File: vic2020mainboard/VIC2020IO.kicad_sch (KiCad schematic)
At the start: 45 parts, among them J10 5v Regulated, J11 Conn_02x08_Odd_Even, J12 Conn_02x22_Row_Letter_First, J13 IEC Port, J14 Joystick 1, J8 Keyboard, J9 LED, SW3 Expansion Port, U21 W65C22NxP, U22 W65C22NxP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

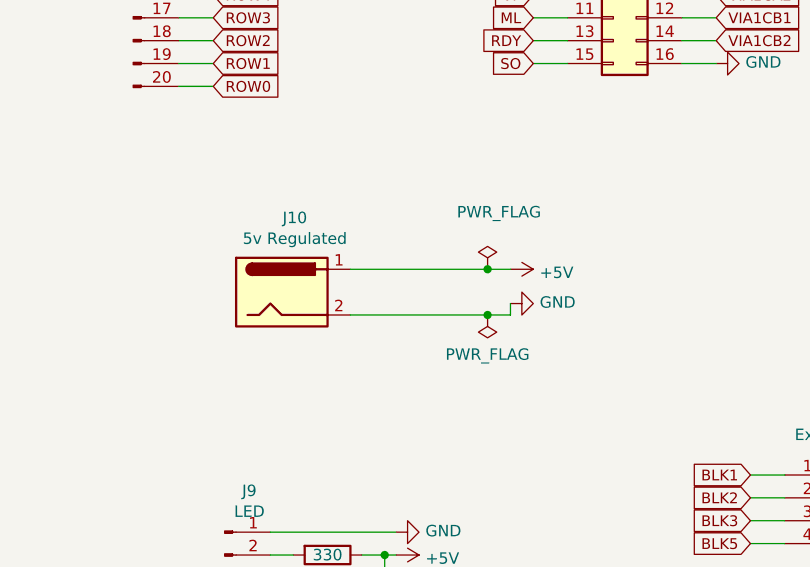
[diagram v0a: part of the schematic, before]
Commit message: Added power supply circuit for 9V AC input
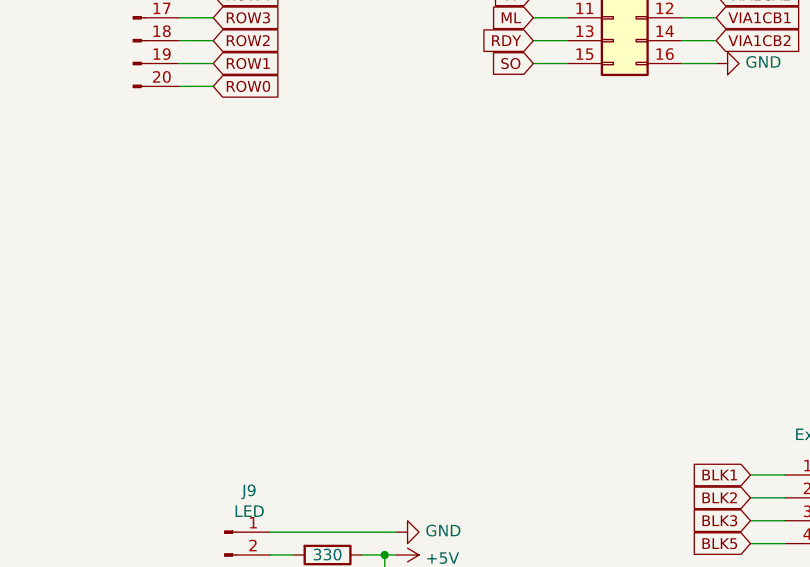
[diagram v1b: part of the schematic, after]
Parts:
- removed J10: 5v Regulated, Connector_BarrelJack:BarrelJack_CUI_PJ-063AH_Horizontal, symbol Connector:Barrel_Jack
